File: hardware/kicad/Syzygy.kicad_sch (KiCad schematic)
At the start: 11 parts, among them U1 ESP32-WROOM-32, U2 INA226

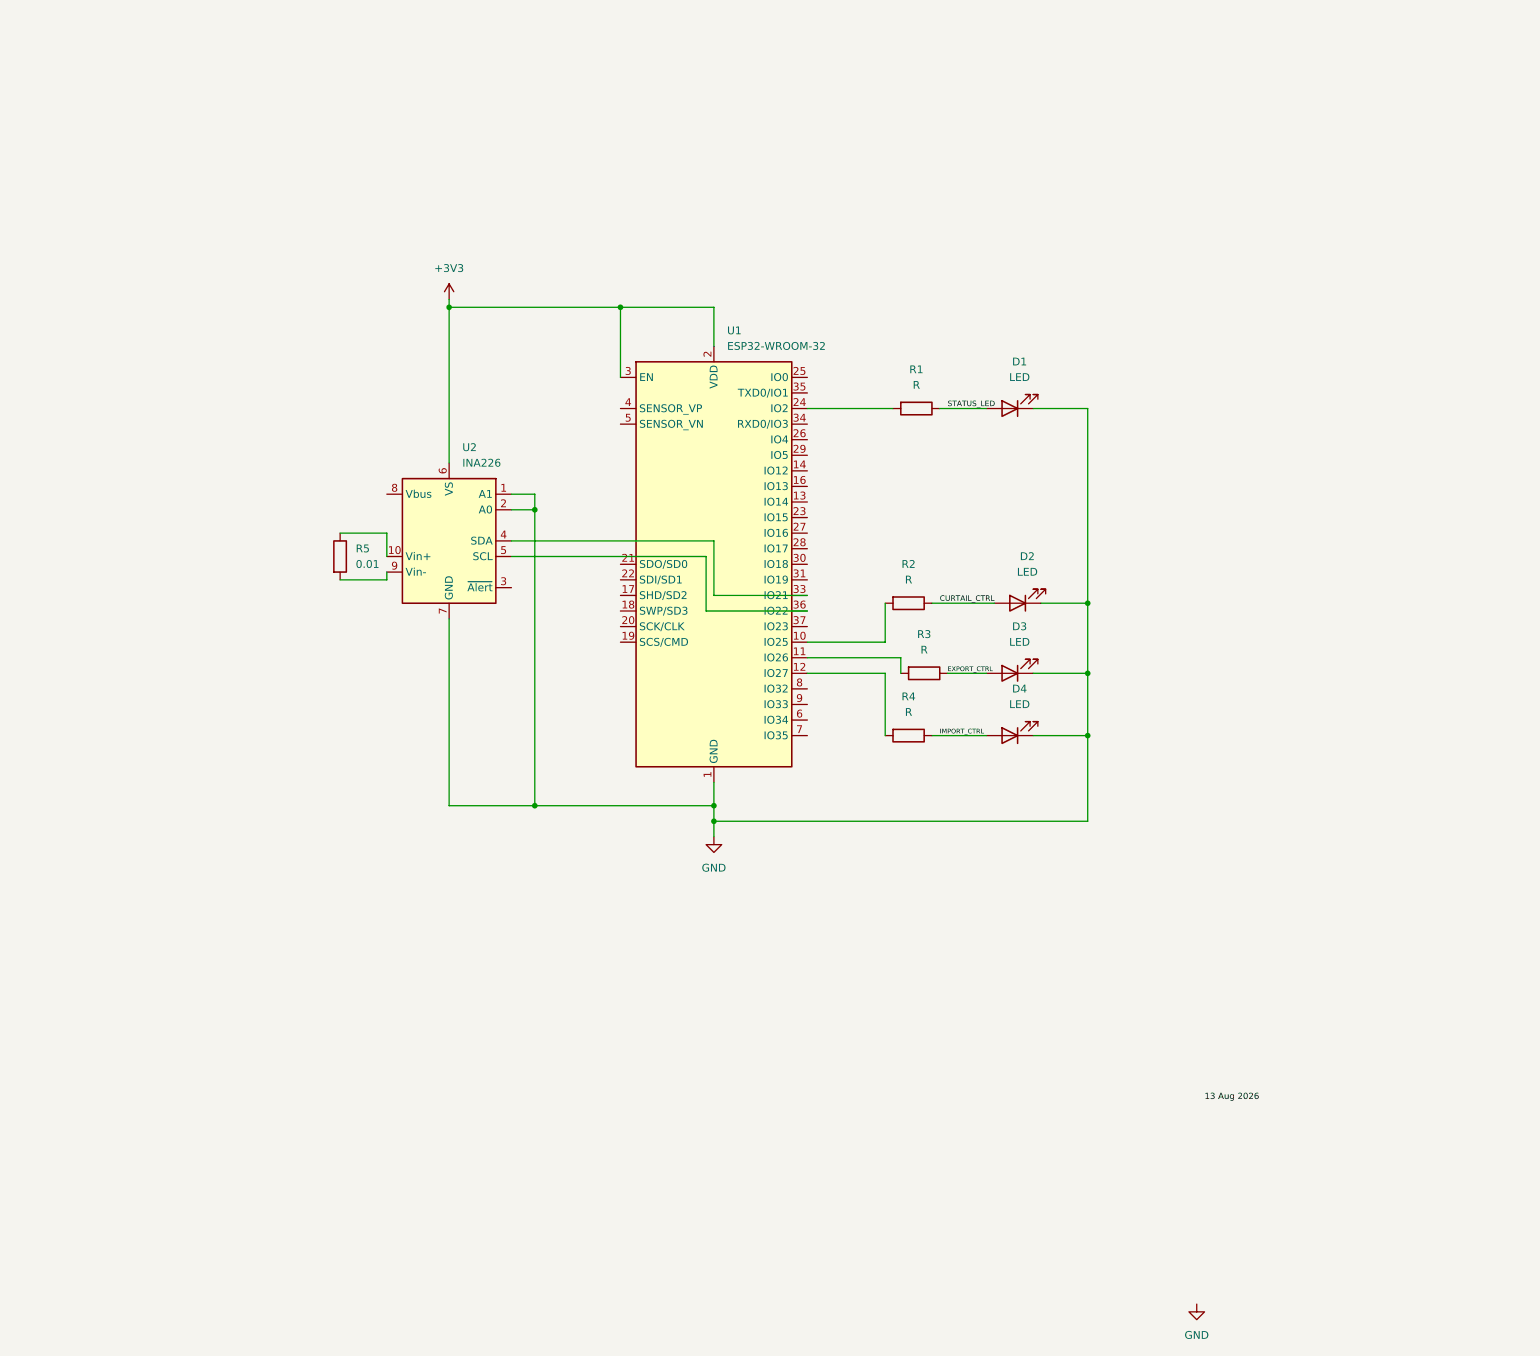
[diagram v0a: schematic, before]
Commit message: update schematic
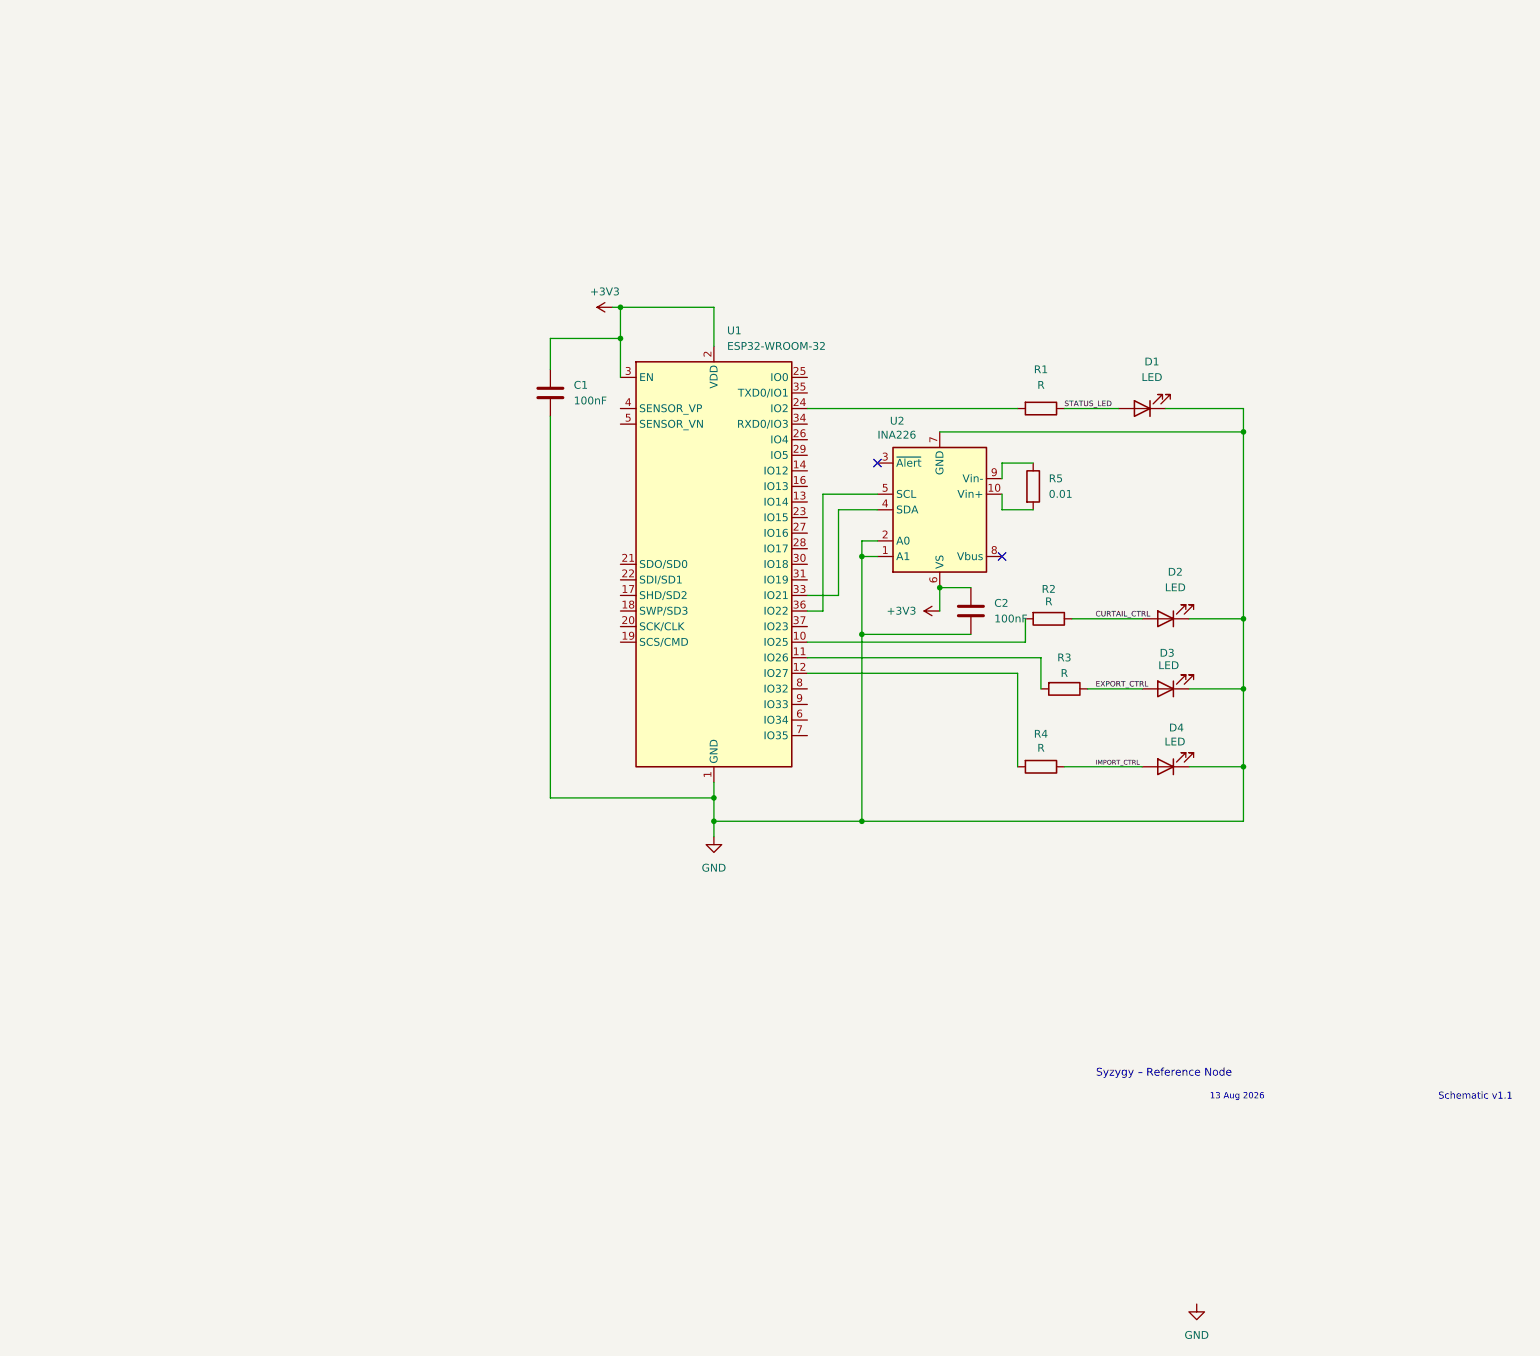
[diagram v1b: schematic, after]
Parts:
- added C1, C2: 100nF, symbol Device:C
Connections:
- net +3V3: now also C1.1, C2.1
- net GND: now also C1.2, C2.2
- net at U2.10 (Vin+): now also R5.2; no longer R5.1
- net at U2.9 (Vin-): now also R5.1; no longer R5.2
- no-connect marks 0 -> 2
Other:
- note added: "13 Aug 2026"
- note added: "Schematic v1.1"
- note added: "Syzygy – Reference Node"
- moved on the sheet: D1, D2, D3, D4, R1, R2, R3, R4, R5, U2

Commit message: update schematic : final version with reverse polarity protection
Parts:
- added D5: D, symbol Device:D
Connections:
- net +3V3: now also D5.2 (A); no longer U1.2 (VDD)
- new net: D5.1 (K), U1.2 (VDD)
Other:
- note added: "28 Aug 2026"
- note added: "Input Protection (concept): - Reverse polarity diode - Fuse / PTC recommended on real hardware"
- note added: "Schematic final"
- note added: "Syzygy - Reference Node Hardware Schematic – Final 28 August 2026"
- note removed: "13 Aug 2026"
- note removed: "Schematic v1.1"
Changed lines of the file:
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@@
 	(generator_version "10.0")
 	(paper "A4")
+	(text "Input Protection (concept):\n- Reverse polarity diode\n- Fuse / PTC recommended \non real hardware"
+		(exclude_from_sim no)
+		(at 142.748 60.452 0)
+		(effects
+			(font
+				(size 1.27 1.27)
+			)
+		)
+	)
 	(text "Syzygy – Reference Node"
 		(exclude_from_sim no)
@@
 		)
 	)
-	(text "Schematic v1.1"
+	(text "Schematic final"
 		(exclude_from_sim no)
 		(at 251.206 193.548 0)
@@
 		)
 	)
-	(text "13 Aug 2026"
+	(text "28 Aug 2026"
 		(exclude_from_sim no)
 		(at 212.344 193.548 0)
@@
 		)
 	)
+	(text "Syzygy - Reference Node\nHardware Schematic – Final \n28 August 2026"
+		(exclude_from_sim no)
+		(at 45.974 23.622 0)
+		(effects
+			(font
+				(size 2.54 2.54)
+			)
+		)
+	)
 	(junction
 		(at 127 144.78)
@@
 	(wire
 		(pts
+			(xy 123.19 64.77) (xy 127 64.77)
+		)
+		(stroke
+			(width 0)
+			(type default)
+		)
+	)
+	(wire
+		(pts
 			(xy 163.83 85.09) (xy 213.36 85.09)
 		)
@@
 	(wire
 		(pts
+			(xy 111.76 64.77) (xy 115.57 64.77)
+		)
+		(stroke
+			(width 0)
+			(type default)
+		)
+	)
+	(wire
+		(pts
 			(xy 147.32 111.76) (xy 142.24 111.76)
 		)
@@
 		(pts
 			(xy 185.42 115.57) (xy 196.85 115.57)
-		)
-		(stroke
-			(width 0)
-			(type default)
-		)
-	)
-	(wire
-		(pts
-			(xy 111.76 64.77) (xy 127 64.77)
 		)
 		(stroke
@@
 	)
 	(symbol
+		(lib_id "Device:D")
+		(at 119.38 64.77 180)
+		(unit 1)
+		(body_style 1)
+		(exclude_from_sim no)
+		(in_bom yes)
+		(on_board yes)
+		(in_pos_files yes)
+		(dnp no)
+		(fields_autoplaced yes)
+		(property "Reference" "D5"
+			(at 119.38 58.42 0)
+			(show_name no)
+			(do_not_autoplace no)
+			(effects
+				(font
+					(size 1.27 1.27)
+				)
+			)
+		)
+		(property "Value" "D"
+			(at 119.38 60.96 0)
+			(show_name no)
+			(do_not_autoplace no)
+			(effects
+				(font
+					(size 1.27 1.27)
+				)
+			)
+		)
+		(property "Footprint" ""
+			(at 119.38 64.77 0)
+			(hide yes)
+			(show_name no)
+			(do_not_autoplace no)
+			(effects
+				(font
+					(size 1.27 1.27)
+				)
+			)
+		)
+		(property "Datasheet" ""
+			(at 119.38 64.77 0)
+			(hide yes)
+			(show_name no)
+			(do_not_autoplace no)
+			(effects
+				(font
+					(size 1.27 1.27)
+				)
+			)
+		)
+		(property "Description" "Diode"
+			(at 119.38 64.77 0)
+			(hide yes)
+			(show_name no)
+			(do_not_autoplace no)
+			(effects
+				(font
+					(size 1.27 1.27)
+				)
+			)
+		)
+		(property "Sim.Device" "D"
+			(at 119.38 64.77 0)
+			(hide yes)
+			(show_name no)
+			(do_not_autoplace no)
+			(effects
+				(font
+					(size 1.27 1.27)
+				)
+			)
+		)
+		(property "Sim.Pins" "1=K 2=A"
+			(at 119.38 64.77 0)
+			(hide yes)
+			(show_name no)
+			(do_not_autoplace no)
+			(effects
+				(font
+					(size 1.27 1.27)
+				)
+			)
+		)
+		(pin "2"
+		)
+		(pin "1"
+		)
+		(instances
+			(project "Syzygy"
+				(path "/e5675157-5847-41f2-89c7-b0a705829b87"
+					(reference "D5")
+					(unit 1)
+				)
+			)
+		)
+	)
+	(symbol
 		(lib_id "power:+3V3")
 		(at 163.83 114.3 90)
@@
 					(unit 1)
 				)
-			)
-		)
-	)
-	(symbol
-		(lib_id "power:GND")
-		(at 205.74 227.33 0)
-		(unit 1)
-		(body_style 1)
-		(exclude_from_sim no)
-		(in_bom yes)
-		(on_board yes)
-		(in_pos_files yes)
-		(dnp no)
-		(fields_autoplaced yes)
-		(property "Reference" "#PWR01"
-			(at 205.74 233.68 0)
-			(hide yes)
-			(show_name no)
-			(do_not_autoplace no)
-			(effects
-				(font
-					(size 1.27 1.27)
-				)
-			)
-		)
-		(property "Value" "GND"
-			(at 205.74 232.41 0)
-			(show_name no)
-			(do_not_autoplace no)
-			(effects
-				(font
-					(size 1.27 1.27)
-				)
-			)
-		)
-		(property "Footprint" ""
-			(at 205.74 227.33 0)
-			(hide yes)
-			(show_name no)
-			(do_not_autoplace no)
-			(effects
-				(font
-					(size 1.27 1.27)
-				)
-			)
-		)
-		(property "Datasheet" ""
-			(at 205.74 227.33 0)
-			(hide yes)
-			(show_name no)
-			(do_not_autoplace no)
-			(effects
-				(font
-					(size 1.27 1.27)
-				)
-			)
-		)
-		(property "Description" "Power symbol creates a global label with name \"GND\" , ground"
-			(at 205.74 227.33 0)
-			(hide yes)
-			(show_name no)
-			(do_not_autoplace no)
-			(effects
-				(font
-					(size 1.27 1.27)
-				)
-			)
-		)
-		(pin "1"
-		)
-		(instances
-			(project "Syzygy"
-				(path "/e5675157-5847-41f2-89c7-b0a705829b87"
-					(reference "#PWR01")
-					(unit 1)
-				)
